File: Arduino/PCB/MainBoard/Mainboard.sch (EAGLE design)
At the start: 58 parts, among them IC1 ULN2803ADW, IC2 DS1338Z-33+, J1 FTDI_DEVICE, J2 FTDI_DEVICE, J3 DC-005, U1 ATMEGA328-AU, U4 R-78B5.0-2.0, X1 16Mhz, X2 32.768kHz

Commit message: Mainboard
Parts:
- removed X2: 32.768kHz, IQD-Frequency-Products:HC49-HC49-3L
- added J4: XBEE CONN, SparkFun-Connectors:FTDI_DEVICE
- added JP3: (no value), jumper:JP2E
- added Q1: 32.768kHz, MainboardComponents:R26-32.768-12.5
- J1: value FTDI_DEVICE -> ARDUINO PROG
- J2: value FTDI_DEVICE -> BOOTL PROG
- R1, R10, R4, R5, R6, R7, R8, R9: value 580 -> 5k3
- renumbered U$1 to DF1, U$2 to DF2, U$3 to DF3, U$4 to DF4, U$5 to DF5, U$6 to DF6, U$7 to DF7, U$8 to DF8
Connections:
- new net N$41: IC2.X1, Q1.2
- new net N$42: J4.CTS, XB1.!RTS!/DIO6
- net +12V: now also IC1.COM
- net +3V3: now also J4.VCC
- net GND: now also J4.GND, JP3.1, XB1.!DTR!/SLEEP_RQ/DIO8; no longer IC1.COM
- net N$13: now also J4.DTR, XB1.!CTS!/DIO7; no longer IC2.X1, X2.1
- net N$14: now also Q1.1; no longer X2.3
- net N$2: now also JP3.2
- net N$3: now also J4.TXO
- net N$35: now also J4.RXI

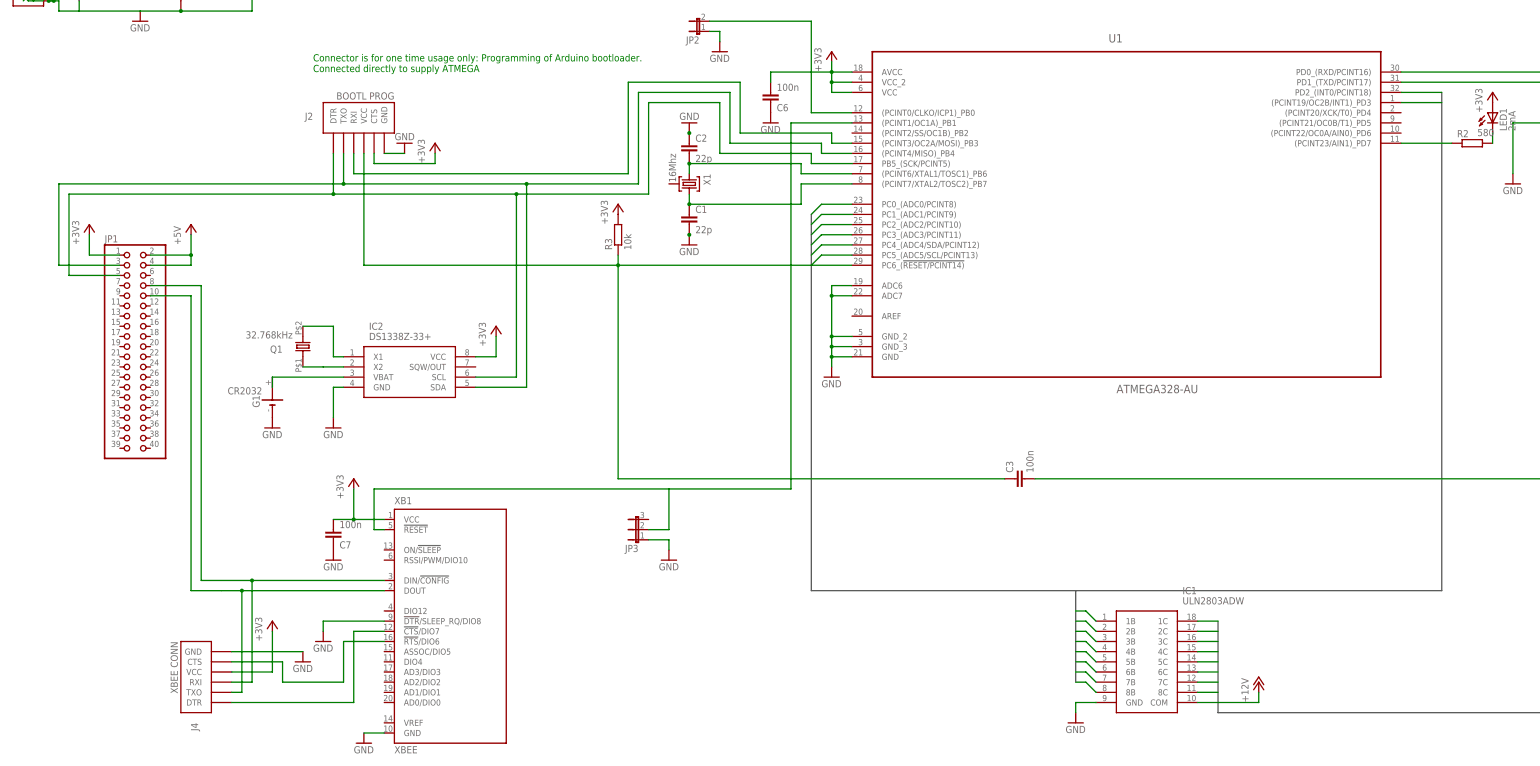
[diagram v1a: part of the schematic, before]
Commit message: 
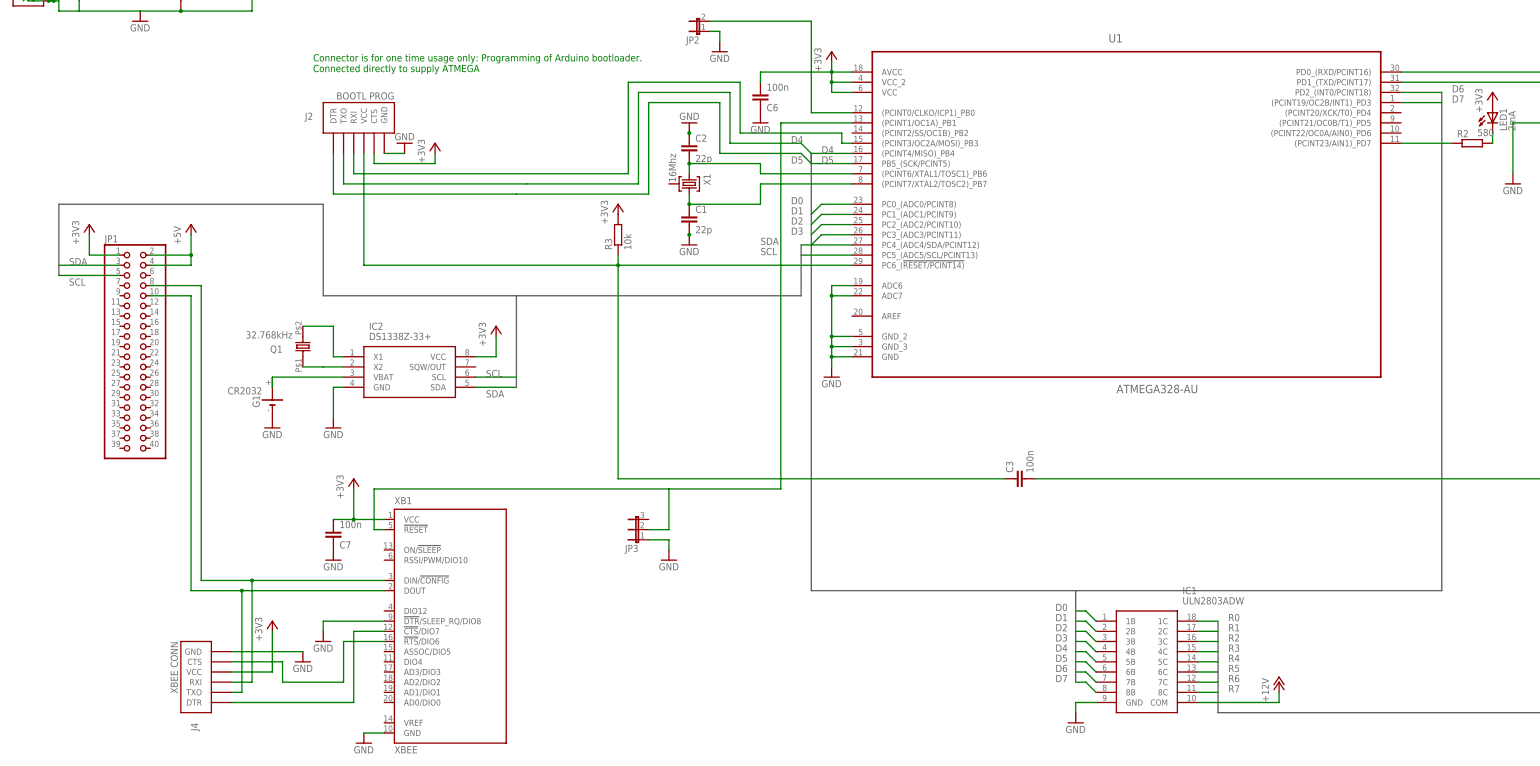
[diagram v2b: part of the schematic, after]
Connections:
- removed net N$23: IC2.SCL, J2.DTR, JP1.5, U1.PB5_(SCK/PCINT5)
- removed net N$24: IC2.SDA, J2.TXO, JP1.3, U1.(PCINT4/MISO)_PB4
- new net SCL: IC2.SCL, JP1.5, U1.PC5_(ADC5/SCL/PCINT13)
- new net SDA: IC2.SDA, JP1.3, U1.PC4_(ADC4/SDA/PCINT12)
- net D4: now also J2.TXO, U1.(PCINT4/MISO)_PB4; no longer U1.PC4_(ADC4/SDA/PCINT12)
- net D5: now also J2.DTR, U1.PB5_(SCK/PCINT5); no longer U1.PC5_(ADC5/SCL/PCINT13)
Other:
- moved on the sheet: C6

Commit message: 
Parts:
- added LED10: 2mA, led:LED3MM
- added R11: 580, rcl:R-EU_R0603
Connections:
- new net N$24: LED10.C, R11.2
- new net N$44: R11.1, U1.(PCINT22/OC0A/AIN0)_PD6
- net +3V3: now also LED10.A
- net N$12: no longer G1.+@1
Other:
- moved on the sheet: LED1, R2
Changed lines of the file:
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@@
 </class>
 <class number="2" name="Relay" width="1.778" drill="0">
-<clearance class="2" value="1.778"/>
 </class>
 </classes>
@@
 <part name="GND17" library="supply1" deviceset="GND" device=""/>
 <part name="P+10" library="supply1" deviceset="+12V" device=""/>
+<part name="R11" library="rcl" deviceset="R-EU_" device="R0603" value="580"/>
+<part name="LED10" library="led" deviceset="LED" device="3MM" value="2mA"/>
 </parts>
 <sheets>
@@
 <attribute name="VALUE" x="177.8" y="27.94" size="1.778" layer="96"/>
 </instance>
-<instance part="LED1" gate="G$1" x="165.1" y="55.88"/>
-<instance part="R2" gate="G$1" x="160.02" y="48.26" smashed="yes">
-<attribute name="NAME" x="156.21" y="49.7586" size="1.778" layer="95"/>
-<attribute name="VALUE" x="161.29" y="50.038" size="1.778" layer="96"/>
+<instance part="LED1" gate="G$1" x="165.1" y="86.36"/>
+<instance part="R2" gate="G$1" x="165.1" y="73.66" smashed="yes" rot="R90">
+<attribute name="NAME" x="163.6014" y="69.85" size="1.778" layer="95" rot="R90"/>
+<attribute name="VALUE" x="163.322" y="74.93" size="1.778" layer="96" rot="R90"/>
 </instance>
 <instance part="R3" gate="G$1" x="-53.34" y="25.4" rot="R90"/>
 <instance part="+3V9" gate="G$1" x="-53.34" y="33.02"/>
 <instance part="C3" gate="G$1" x="45.72" y="-35.56" rot="R90"/>
-<instance part="P+4" gate="G$1" x="165.1" y="60.96"/>
+<instance part="P+4" gate="G$1" x="165.1" y="96.52"/>
 <instance part="P+5" gate="G$1" x="0" y="71.12"/>
 <instance part="J2" gate="G$1" x="-119.38" y="50.8" smashed="yes" rot="R90">
@@
 <instance part="GND17" gate="1" x="-40.64" y="-55.88"/>
 <instance part="P+10" gate="1" x="111.76" y="-86.36"/>
+<instance part="R11" gate="G$1" x="157.48" y="73.66" smashed="yes" rot="R90">
+<attribute name="NAME" x="155.9814" y="69.85" size="1.778" layer="95" rot="R90"/>
+<attribute name="VALUE" x="155.702" y="74.93" size="1.778" layer="96" rot="R90"/>
+</instance>
+<instance part="LED10" gate="G$1" x="157.48" y="86.36"/>
 </instances>
 <busses>
@@
 <wire x1="-195.58" y1="86.36" x2="-193.04" y2="86.36" width="0.1524" layer="91"/>
 <junction x="-193.04" y="86.36"/>
+<junction x="-187.96" y="81.28"/>
+<junction x="-172.72" y="81.28"/>
 </segment>
 <segment>
@@
 </segment>
 <segment>
-<pinref part="P+4" gate="G$1" pin="+3V3"/>
-<pinref part="LED1" gate="G$1" pin="A"/>
-</segment>
-<segment>
 <pinref part="P+3" gate="G$1" pin="+3V3"/>
 <wire x1="-83.82" y1="0" x2="-83.82" y2="-5.08" width="0.1524" layer="91"/>
@@
 <pinref part="P+9" gate="G$1" pin="+3V3"/>
 <wire x1="-139.7" y1="-83.82" x2="-139.7" y2="-73.66" width="0.1524" layer="91"/>
+</segment>
+<segment>
+<pinref part="LED1" gate="G$1" pin="A"/>
+<pinref part="P+4" gate="G$1" pin="+3V3"/>
+<wire x1="165.1" y1="88.9" x2="165.1" y2="91.44" width="0.1524" layer="91"/>
+<pinref part="LED10" gate="G$1" pin="A"/>
+<wire x1="165.1" y1="91.44" x2="165.1" y2="93.98" width="0.1524" layer="91"/>
+<wire x1="157.48" y1="88.9" x2="157.48" y2="91.44" width="0.1524" layer="91"/>
+<wire x1="157.48" y1="91.44" x2="165.1" y2="91.44" width="0.1524" layer="91"/>
+<junction x="165.1" y="91.44"/>
 </segment>
 </net>
@@
 <label x="236.22" y="53.34" size="1.778" layer="95"/>
 <junction x="228.6" y="53.34"/>
-</segment>
-</net>
-<net name="N$8" class="0">
-<segment>
-<pinref part="LED1" gate="G$1" pin="C"/>
-<pinref part="R2" gate="G$1" pin="2"/>
-<wire x1="165.1" y1="50.8" x2="165.1" y2="48.26" width="0.1524" layer="91"/>
-</segment>
-</net>
-<net name="N$11" class="0">
-<segment>
-<pinref part="U1" gate="A" pin="(PCINT23/AIN1)_PD7"/>
-<pinref part="R2" gate="G$1" pin="1"/>
-<wire x1="142.24" y1="48.26" x2="154.94" y2="48.26" width="0.1524" layer="91"/>
-</segment>
-</net>
-<net name="N$12" class="0">
-<segment>
-<pinref part="IC2" gate="G$1" pin="VBAT"/>
-<pinref part="G1" gate="1" pin="+"/>
-<wire x1="-121.92" y1="-10.16" x2="-139.7" y2="-10.16" width="0.1524" layer="91"/>
-<pinref part="G1" gate="1" pin="+@1"/>
-<wire x1="-139.7" y1="-10.16" x2="-139.7" y2="-12.7" width="0.1524" layer="91"/>
 </segment>
 </net>
@@
 <pinref part="C4" gate="G$1" pin="1"/>
 <wire x1="-187.96" y1="91.44" x2="-187.96" y2="93.98" width="0.1524" layer="91"/>
+<junction x="-187.96" y="93.98"/>
 </segment>
 <segment>
@@
 </segment>
 </net>
-<net name="N$32" class="2">
-<segment>
-<pinref part="REL7" gate="G$1" pin="NO"/>
-<wire x1="269.24" y1="-73.66" x2="302.26" y2="-73.66" width="0.1524" layer="91"/>
-<wire x1="302.26" y1="-73.66" x2="302.26" y2="-45.72" width="0.1524" layer="91"/>
-<pinref part="X4" gate="-8" pin="KL"/>
-<wire x1="302.26" y1="-45.72" x2="304.8" y2="-45.72" width="0.1524" layer="91"/>
-</segment>
-</net>
 <net name="N$33" class="2">
 <segment>
@@
 <pinref part="JP3" gate="1" pin="2"/>
 <wire x1="-40.64" y1="-48.26" x2="-45.72" y2="-48.26" width="0.1524" layer="91"/>
+<junction x="-40.64" y="-38.1"/>
 </segment>
 </net>
@@
 </segment>
 </net>
+<net name="N$12" class="0">
+<segment>
+<pinref part="IC2" gate="G$1" pin="VBAT"/>
+<pinref part="G1" gate="1" pin="+"/>
+<wire x1="-121.92" y1="-10.16" x2="-139.7" y2="-10.16" width="0.1524" layer="91"/>
+</segment>
+</net>
+<net name="N$8" class="0">
+<segment>
+<pinref part="U1" gate="A" pin="(PCINT23/AIN1)_PD7"/>
+<wire x1="142.24" y1="48.26" x2="165.1" y2="48.26" width="0.1524" layer="91"/>
+<pinref part="R2" gate="G$1" pin="1"/>
+<wire x1="165.1" y1="48.26" x2="165.1" y2="68.58" width="0.1524" layer="91"/>
+</segment>
+</net>
+<net name="N$11" class="0">
+<segment>
+<pinref part="R2" gate="G$1" pin="2"/>
+<pinref part="LED1" gate="G$1" pin="C"/>
+<wire x1="165.1" y1="78.74" x2="165.1" y2="81.28" width="0.1524" layer="91"/>
+</segment>
+</net>
+<net name="N$24" class="0">
+<segment>
+<pinref part="LED10" gate="G$1" pin="C"/>
+<pinref part="R11" gate="G$1" pin="2"/>
+<wire x1="157.48" y1="81.28" x2="157.48" y2="78.74" width="0.1524" layer="91"/>
+</segment>
+</net>
+<net name="N$44" class="0">
+<segment>
+<pinref part="R11" gate="G$1" pin="1"/>
+<wire x1="157.48" y1="68.58" x2="157.48" y2="50.8" width="0.1524" layer="91"/>
+<pinref part="U1" gate="A" pin="(PCINT22/OC0A/AIN0)_PD6"/>
+<wire x1="157.48" y1="50.8" x2="142.24" y2="50.8" width="0.1524" layer="91"/>
+</segment>
+</net>
+<net name="N$23" class="2">
+<segment>
+<pinref part="X4" gate="-8" pin="KL"/>
+<wire x1="304.8" y1="-45.72" x2="302.26" y2="-45.72" width="0.1524" layer="91"/>
+<wire x1="302.26" y1="-45.72" x2="302.26" y2="-73.66" width="0.1524" layer="91"/>
+<pinref part="REL7" gate="G$1" pin="NO"/>
+<wire x1="302.26" y1="-73.66" x2="269.24" y2="-73.66" width="0.1524" layer="91"/>
+</segment>
+</net>

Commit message: as send to allpcb
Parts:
- removed G1: CR2032, MainboardComponents:BATTERY_CR2032H
- added U$1: KEYSTONE_1066, MainboardComponents:KEYSTONE_1066
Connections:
- net GND: now also U$1.-; no longer G1.-
- net N$12: now also U$1.+; no longer G1.+
- net R0: now also DF1.A, LED2.C, REL0.A2; no longer DF8.A, LED9.C, REL7.A2
- net R1: now also DF2.A, LED3.C, REL1.A2; no longer DF7.A, LED8.C, REL6.A2
- net R2: now also DF3.A, LED4.C, REL2.A2; no longer DF6.A, LED7.C, REL5.A2
- net R3: now also DF4.A, LED5.C, REL3.A2; no longer DF5.A, LED6.C, REL4.A2
- net R4: now also DF5.A, LED6.C, REL4.A2; no longer DF4.A, LED5.C, REL3.A2
- net R5: now also DF6.A, LED7.C, REL5.A2; no longer DF3.A, LED4.C, REL2.A2
- net R6: now also DF7.A, LED8.C, REL6.A2; no longer DF2.A, LED3.C, REL1.A2
- net R7: now also DF8.A, LED9.C, REL7.A2; no longer DF1.A, LED2.C, REL0.A2
